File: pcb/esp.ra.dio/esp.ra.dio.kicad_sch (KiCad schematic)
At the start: 34 parts, among them J1 A, J10 UART, J2 B, J3 C, J4 D, J5 START, J6 SELECT, J7 JOY, J8 USB_B_Micro, J9 BATTERY, Q1 BSS138, SW1 POWER, SW2 RESET, SW3 BOOT, U2 VCC, U3 RT9080-33GJ5

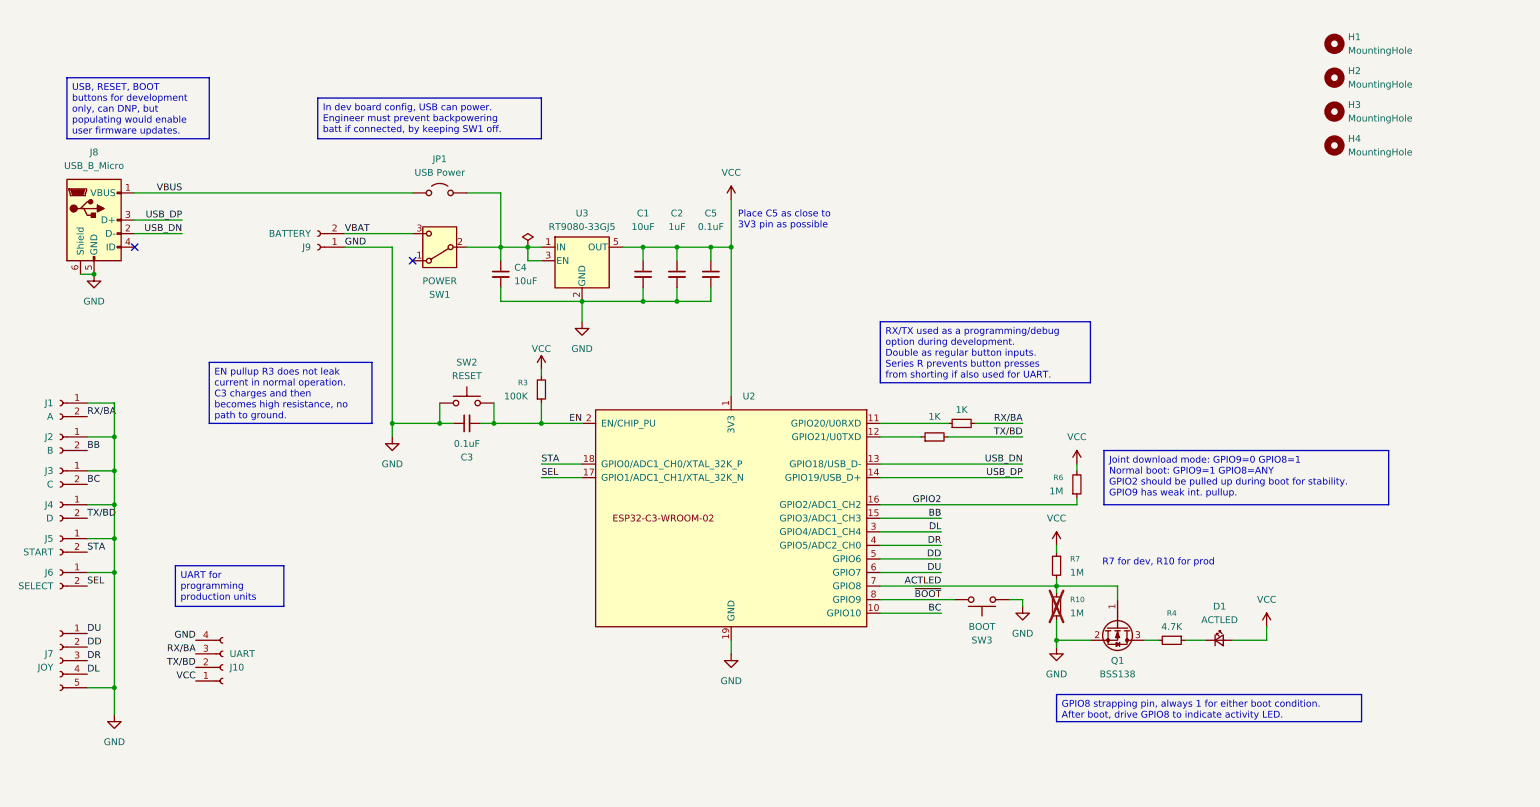
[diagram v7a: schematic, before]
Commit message: Re-splitting RX/BA nets
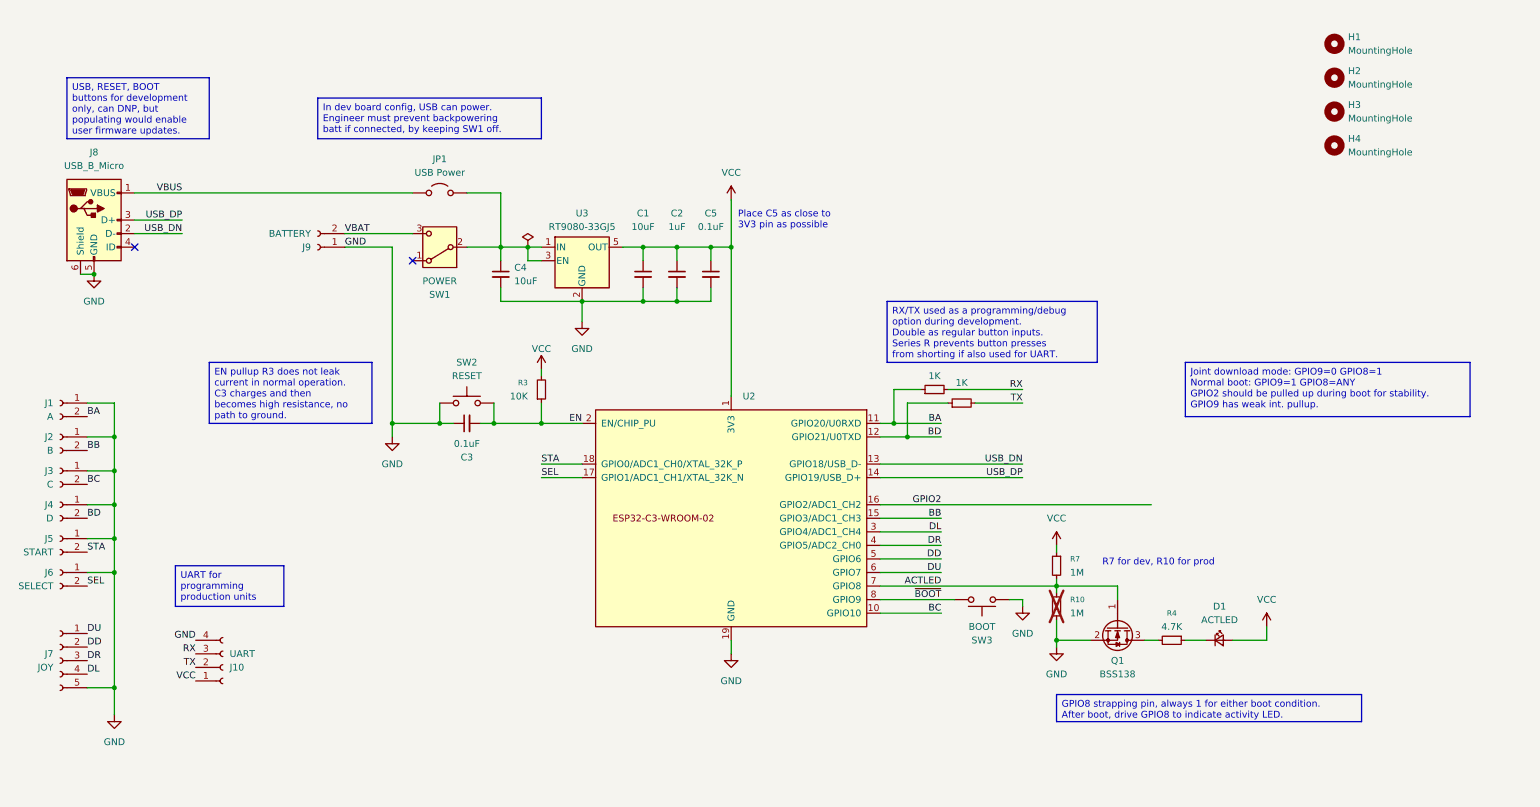
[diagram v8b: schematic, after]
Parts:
- removed R6: 1M, Resistor_SMD:R_0805_2012Metric_Pad1.20x1.40mm_HandSolder, symbol Device:R_Small
- R3: value 100K -> 10K
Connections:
- net BA: now reaches R8.1, U2.11 (GPIO20/U0RXD)
- net BA: now also J1.2 (Pin_2)
- net BD: now reaches R9.1, U2.12 (GPIO21/U0TXD)
- net BD: now also J4.2 (Pin_2)
- net RX/BA renamed RX
- net RX: no longer J1.2 (Pin_2)
- net TX/BD renamed TX
- net TX: no longer J4.2 (Pin_2)
